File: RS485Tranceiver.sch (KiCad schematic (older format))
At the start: 19 parts, among them J10 Conn_01x02, U13 SN75176AD

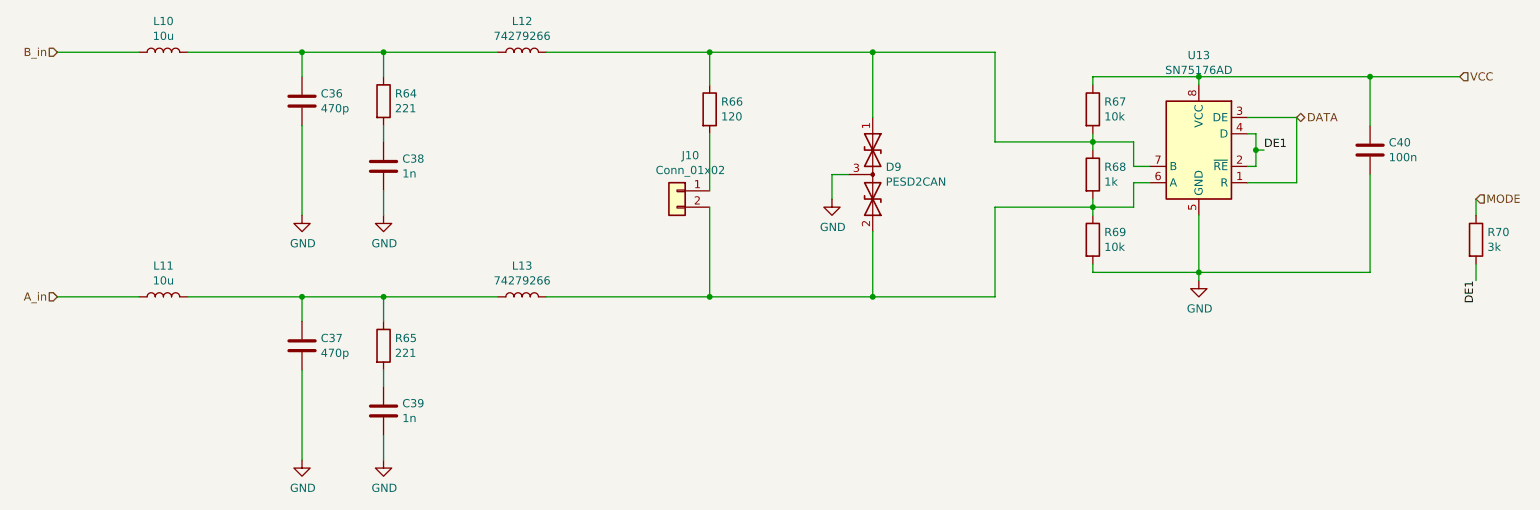
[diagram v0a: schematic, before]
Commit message: rx tx fix, filter mirrored
switched rx/tx signals
filters were mirrored
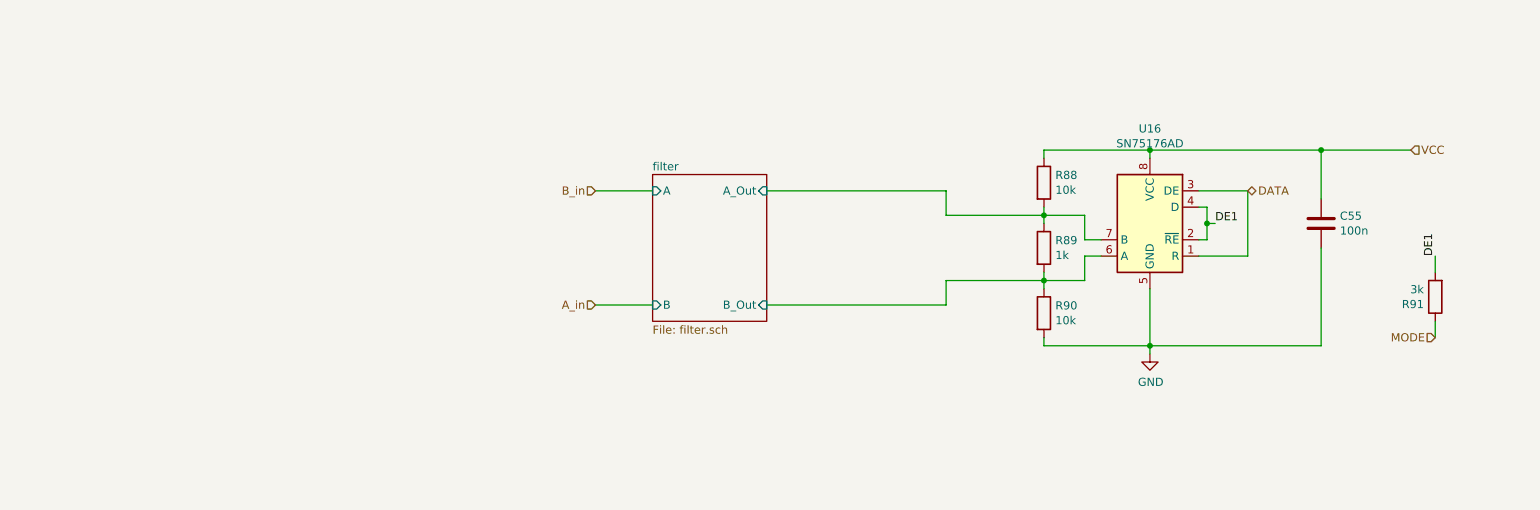
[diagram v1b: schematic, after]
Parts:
- removed C36, C37: 470p, Capacitor_SMD:C_0603_1608Metric, symbol AR2ISS:C
- removed C38, C39: 1n, Capacitor_SMD:C_0603_1608Metric, symbol AR2ISS:C
- removed D9: PESD2CAN, Package_TO_SOT_SMD:SOT-23_Handsoldering, symbol Device:D_TVS_x2_AAC
- removed J10: Conn_01x02, Connector_PinHeader_2.54mm:PinHeader_1x02_P2.54mm_Vertical, symbol Connector_Generic:Conn_01x02
- removed L10, L11: 10u, Inductor_SMD:L_0603_1608Metric, symbol Device:L
- removed L12, L13: 74279266, Inductor_SMD:L_0603_1608Metric, symbol Device:L
- removed R64, R65: 221, Resistor_SMD:R_0603_1608Metric, symbol AR2ISS:R
- removed R66: 120, Resistor_SMD:R_0603_1608Metric, symbol AR2ISS:R
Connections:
- net filter/B_Out: now reaches R68.2, R69.1, U13.6 (A)
- net filter/A_Out: now reaches R67.2, R68.1, U13.7 (B)
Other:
- moved on the sheet: C55, R88, R89, R90, R91, U16

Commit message: ready for ordering
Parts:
- R67, R69: value 10k -> NB
- R68: value 1k -> NB
- U13: value SN75176AD -> SN65HVD3082; symbol Interface_UART:SN75176AD -> AR2ISS:SP3485
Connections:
- net DATA: now also U13.4 (DI); no longer U13.3 (DE)
- net DE1: now also U13.3 (DE); no longer U13.4 (D)
- net filter/A_Out: now also U13.6 (A); no longer U13.7 (B)
- net filter/B_Out: now also U13.7 (B); no longer U13.6 (A)
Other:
- moved on the sheet: U13
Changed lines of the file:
@@
 $Descr A4 11693 8268
 encoding utf-8
-Sheet 18 21
+Sheet 20 21
 Title ""
 Date ""
@@
 $EndDescr
 $Comp
-L Interface_UART:SN75176AD U?
-U 1 1 6072BD51
-P 8300 2850
-AR Path="/606DDE00/6072BD51" Ref="U?"  Part="1"
-AR Path="/6072BD51" Ref="U?"  Part="1"
-AR Path="/60A6CF0D/6072BD51" Ref="U?"  Part="1"
-AR Path="/608A378A/6072BD51" Ref="U?"  Part="1"
-AR Path="/6072829D/6072BD51" Ref="U?"  Part="1"
-AR Path="/6072829D/60727BD1/6072BD51" Ref="U13"  Part="1"
-AR Path="/6072829D/607938CE/6072BD51" Ref="U16"  Part="1"
-AR Path="/6072829D/60795F15/6072BD51" Ref="U14"  Part="1"
-AR Path="/6072829D/60797D2F/6072BD51" Ref="U15"  Part="1"
-F 0 "U16" H 8300 3431 50  0000 C CNN
-F 1 "SN75176AD" H 8300 3340 50  0000 C CNN
-F 2 "Package_SO:SOIC-8_3.9x4.9mm_P1.27mm" H 8300 2350 50  0001 C CNN
-F 3 "http://www.ti.com/lit/ds/symlink/sn75176a.pdf" H 9900 2650 50  0001 C CNN
-	1    8300 2850
-	-1   0    0    -1
-$EndComp
-$Comp
 L AR2ISS:R R?
 U 1 1 6072BD57
@@
 AR Path="/6072829D/60795F15/6072BD57" Ref="R76"  Part="1"
 AR Path="/6072829D/60797D2F/6072BD57" Ref="R83"  Part="1"
-F 0 "R90" H 7720 3446 50  0000 L CNN
-F 1 "10k" H 7720 3355 50  0000 L CNN
+F 0 "R69" H 7720 3446 50  0000 L CNN
+F 1 "NB" H 7720 3355 50  0000 L CNN
 F 2 "Resistor_SMD:R_0603_1608Metric" V 7580 3400 50  0001 C CNN
 F 3 "~" H 7650 3400 50  0001 C CNN
@@
 AR Path="/6072829D/60795F15/6072BD5D" Ref="R77"  Part="1"
 AR Path="/6072829D/60797D2F/6072BD5D" Ref="R84"  Part="1"
-F 0 "R91" H 10120 3346 50  0000 L CNN
+F 0 "R70" H 10120 3346 50  0000 L CNN
 F 1 "3k" H 10120 3255 50  0000 L CNN
 F 2 "Resistor_SMD:R_0603_1608Metric" V 9980 3300 50  0001 C CNN
@@
 AR Path="/6072829D/60795F15/6072BD63" Ref="R74"  Part="1"
 AR Path="/6072829D/60797D2F/6072BD63" Ref="R81"  Part="1"
-F 0 "R88" H 7720 2646 50  0000 L CNN
-F 1 "10k" H 7720 2555 50  0000 L CNN
+F 0 "R67" H 7720 2646 50  0000 L CNN
+F 1 "NB" H 7720 2555 50  0000 L CNN
 F 2 "Resistor_SMD:R_0603_1608Metric" V 7580 2600 50  0001 C CNN
 F 3 "~" H 7650 2600 50  0001 C CNN
@@
 AR Path="/6072829D/60795F15/6072BD6B" Ref="#PWR0116"  Part="1"
 AR Path="/6072829D/60797D2F/6072BD6B" Ref="#PWR0122"  Part="1"
-F 0 "#PWR0130" H 8300 3400 50  0001 C CNN
+F 0 "#PWR0110" H 8300 3400 50  0001 C CNN
 F 1 "GND" H 8305 3477 50  0000 C CNN
 F 2 "" H 8300 3650 50  0001 C CNN
@@
 Wire Wire Line
 	7650 2800 7900 2800
-Wire Wire Line
-	7900 2800 7900 2950
-Wire Wire Line
-	7900 2950 8000 2950
 Connection ~ 7650 2800
 Wire Wire Line
@@
 Wire Wire Line
 	7650 3200 7900 3200
-Wire Wire Line
-	7900 3200 7900 3050
-Wire Wire Line
-	7900 3050 8000 3050
 Connection ~ 7650 3200
 Wire Wire Line
@@
 Wire Wire Line
 	8300 3600 8300 3650
-Wire Wire Line
-	8300 3250 8300 3600
 Connection ~ 8300 3600
 Wire Wire Line
@@
 	7650 2400 8300 2400
 Wire Wire Line
-	8300 2400 8300 2450
-Wire Wire Line
-	8600 2750 8650 2750
-Wire Wire Line
-	8650 2750 8650 2850
-Wire Wire Line
-	8650 2950 8600 2950
-Wire Wire Line
-	8650 2850 8700 2850
-Connection ~ 8650 2850
-Wire Wire Line
-	8650 2850 8650 2950
-Text Label 8700 2850 0    50   ~ 0
+	8700 2900 8750 2900
+Wire Wire Line
+	8750 2900 8750 3000
+Wire Wire Line
+	8750 3100 8700 3100
+Wire Wire Line
+	8750 3000 8800 3000
+Connection ~ 8750 3000
+Wire Wire Line
+	8750 3000 8750 3100
+Text Label 8800 3000 0    50   ~ 0
 DE1
 Wire Wire Line
-	8900 2650 8900 3050
-Wire Wire Line
-	8600 2650 8900 2650
-Wire Wire Line
-	8600 3050 8900 3050
+	9000 2800 9000 3200
+Wire Wire Line
+	8700 2800 9000 2800
+Wire Wire Line
+	8700 3200 9000 3200
 Text Label 10050 3050 1    50   ~ 0
 DE1
@@
 AR Path="/6072829D/60795F15/6072BD8E" Ref="C45"  Part="1"
 AR Path="/6072829D/60797D2F/6072BD8E" Ref="C50"  Part="1"
-F 0 "C55" H 9465 2896 50  0000 L CNN
+F 0 "C40" H 9465 2896 50  0000 L CNN
 F 1 "100n" H 9465 2805 50  0000 L CNN
 F 2 "Capacitor_SMD:C_0603_1608Metric" H 9388 2700 50  0001 C CNN
@@
 AR Path="/6072829D/60795F15/6072BDA0" Ref="R75"  Part="1"
 AR Path="/6072829D/60797D2F/6072BDA0" Ref="R82"  Part="1"
-F 0 "R89" H 7720 3046 50  0000 L CNN
-F 1 "1k" H 7720 2955 50  0000 L CNN
+F 0 "R68" H 7720 3046 50  0000 L CNN
+F 1 "NB" H 7720 2955 50  0000 L CNN
 F 2 "Resistor_SMD:R_0603_1608Metric" V 7580 3000 50  0001 C CNN
 F 3 "~" H 7650 3000 50  0001 C CNN
@@
 Text HLabel 9900 2400 2    50   Input ~ 0
 VCC
-Text HLabel 8900 2650 2    50   BiDi ~ 0
+Text HLabel 9000 2800 2    50   BiDi ~ 0
 DATA
 Text HLabel 4900 3350 0    50   Input ~ 0
@@
 Wire Wire Line
 	4900 2650 5250 2650
+$Comp
+L AR2ISS:SP3485 U?
+U 1 1 6072BD51
+P 8300 3000
+AR Path="/606DDE00/6072BD51" Ref="U?"  Part="1"
+AR Path="/6072BD51" Ref="U?"  Part="1"
+AR Path="/60A6CF0D/6072BD51" Ref="U?"  Part="1"
+AR Path="/608A378A/6072BD51" Ref="U?"  Part="1"
+AR Path="/6072829D/6072BD51" Ref="U?"  Part="1"
+AR Path="/6072829D/60727BD1/6072BD51" Ref="U13"  Part="1"
+AR Path="/6072829D/607938CE/6072BD51" Ref="U16"  Part="1"
+AR Path="/6072829D/60795F15/6072BD51" Ref="U14"  Part="1"
+AR Path="/6072829D/60797D2F/6072BD51" Ref="U15"  Part="1"
+F 0 "U13" H 8300 3581 50  0000 C CNN
+F 1 "SN65HVD3082" H 8300 3490 50  0000 C CNN
+F 2 "Package_SO:SOIC-8_3.9x4.9mm_P1.27mm" H 8300 2500 50  0001 C CNN
+F 3 "http://www.ti.com/lit/ds/symlink/sn75176a.pdf" H 9900 2800 50  0001 C CNN
+	1    8300 3000
+	-1   0    0    -1
+$EndComp
+Wire Wire Line
+	8300 3400 8300 3600
+Wire Wire Line
+	8300 2400 8300 2600
+Wire Wire Line
+	7900 2900 7900 2800
+Wire Wire Line
+	7900 3100 7900 3200
 $EndSCHEMATC
